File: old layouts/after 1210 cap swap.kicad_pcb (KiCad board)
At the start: 4 copper layers, 65 x 56 mm, 189 parts, among them J101 Conn_01x01, J102 Conn_01x01, J1101 USB_C_Receptacle, J401 +Vbat, J402 Gnd, J403 A, J404 B, J405 C, J406 Conn_01x03, K101 SERVO, P101 CANBUS, P102 CTRL_SIGNALS, P103 Serial1/tim4, P104 I2C, P106 HALL/Encoder, P801 SWD_DEBUG, P901 I2C, Q401 Q_PNP_BCE, Q501 TPH2R608NH,L1Q, Q502 TPH2R608NH,L1Q, Q503 TPH2R608NH,L1Q, Q504 TPH2R608NH,L1Q, Q601 TPH2R608NH,L1Q, Q602 TPH2R608NH,L1Q, Q603 TPH2R608NH,L1Q, Q604 TPH2R608NH,L1Q, Q701 TPH2R608NH,L1Q, Q702 TPH2R608NH,L1Q, Q703 TPH2R608NH,L1Q, Q704 TPH2R608NH,L1Q, SW801 SW_Push, U201 MAX3051, U301 TPS561201, U401 DRV8353RSRGZT, U801 STM32F40X_LQFP64, X801 8MHz 10ppm, X802 8MHz 10ppm

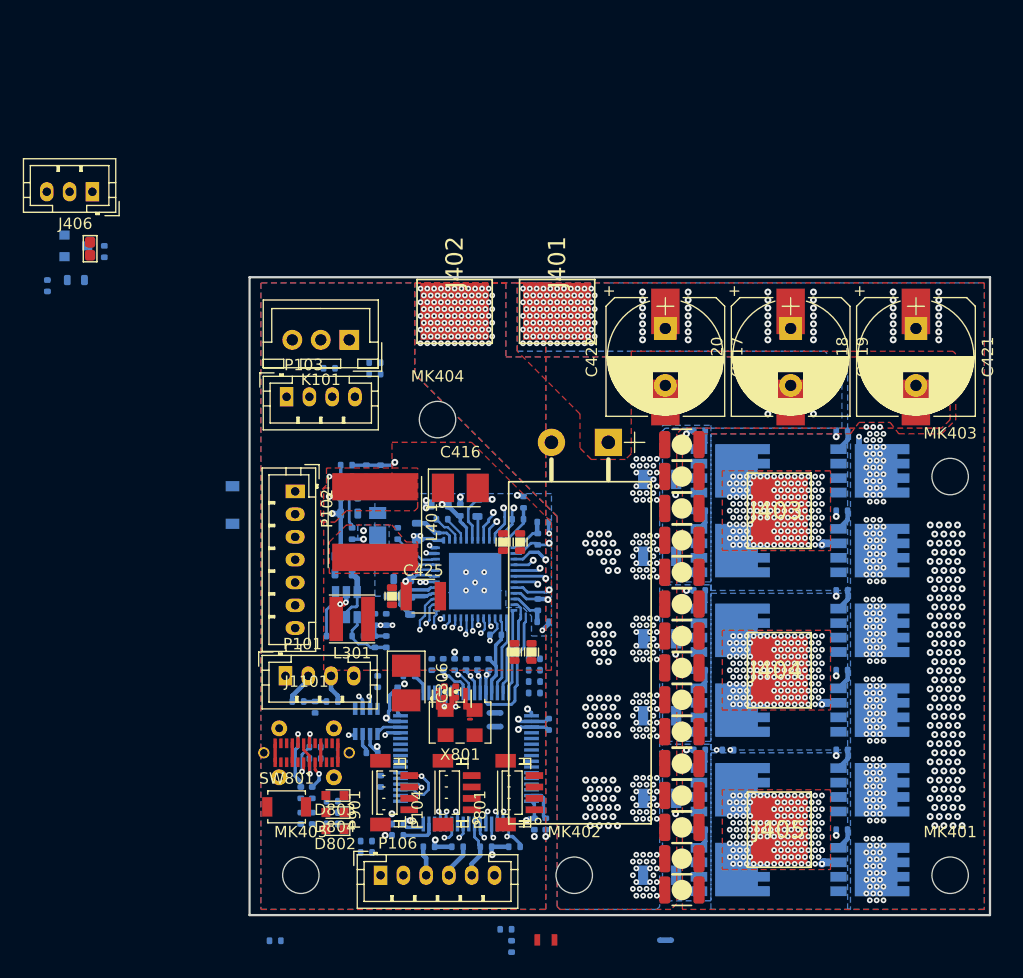
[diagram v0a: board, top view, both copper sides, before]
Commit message: connector layout basically finalised. drv gate layout finished mcu layout starting
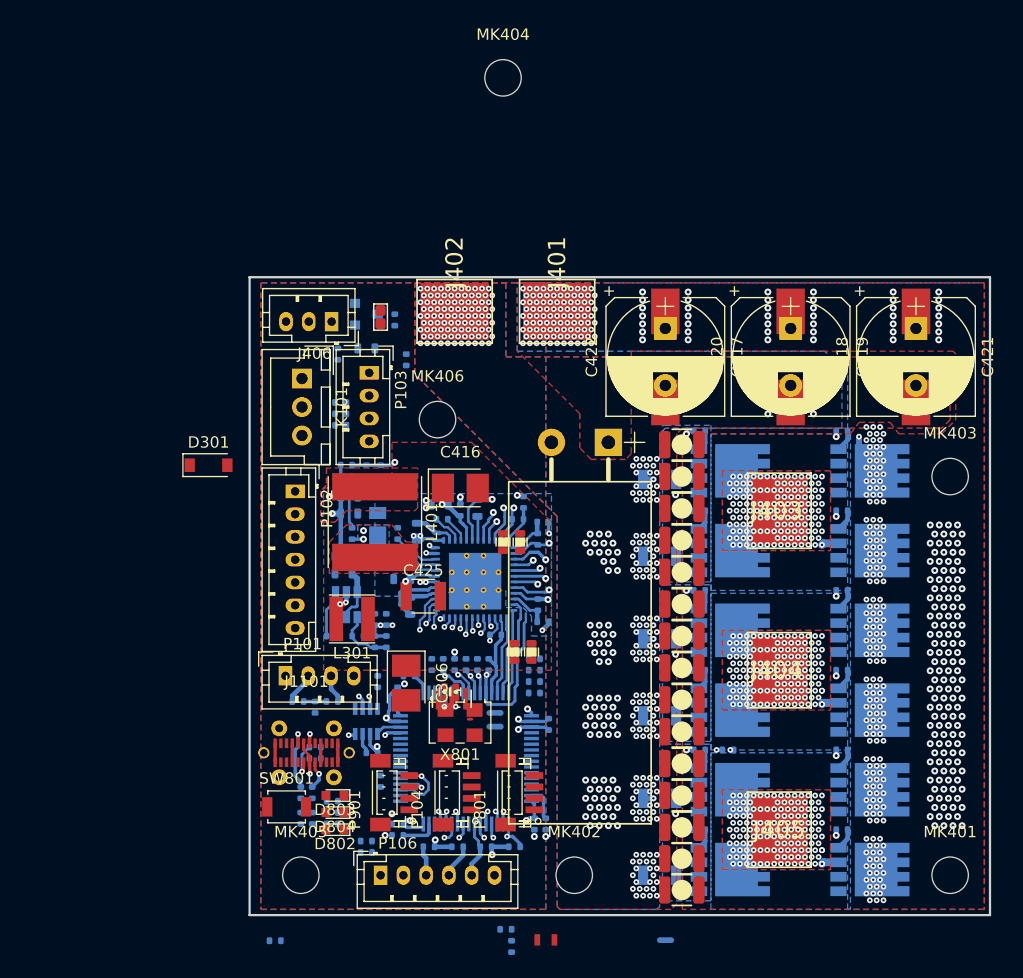
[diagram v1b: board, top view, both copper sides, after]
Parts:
- removed R421: 0Ω, pkl_dipol:R_0603
- added MK406: Mounting_Hole, Mounting_Holes:MountingHole_3.2mm_M3_DIN965, F.Cu at (121.0, 116.0)
- D301: moved to F.Cu
- R418: value 1M -> 10k
- moved MK404 30.5 mm to (126.8, 86.0)
- moved JP401 26.2 mm to (116.0, 107.0)
- moved Q401 26.2 mm to (114.8, 106.8)
- moved R418 26.2 mm to (117.2, 107.2)
- moved R419 26.2 mm to (114.8, 109.8)
- moved R420 26.2 mm to (112.2, 110.2)
- moved J406 23.9 mm to (111.7, 107.4)
- moved R403 20.8 mm to (118.2, 110.8), turned to 270 degrees
- moved P103 7.55 mm to (115.0, 111.9), turned to 270 degrees
- moved K101 5.36 mm to (109.1, 112.4), turned to 270 degrees
- moved R101 5.10 mm to (112.5, 116.5)
- moved C101 4.61 mm to (112.5, 115.5)
- moved R102 4.61 mm to (112.5, 114.5)
- moved D301 4.08 mm to (100.9, 120.0), turned to 0 degrees
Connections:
- net /ADC_BRAKE_R renamed Net-(P102-Pad4)
- net /ADC_THROTTLE_R renamed Net-(P102-Pad3)
- C404 pad 1: /drv_power_stage/BK_VIN -> +BATT
- C425 pad 1: /drv_power_stage/BK_VIN -> +BATT
- R403 pad 1: /drv_power_stage/BK_VIN -> /drv_power_stage/batt_pwr_ctl
- U401 pad 43: /drv_power_stage/BK_VIN -> +BATT
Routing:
- net /drv_power_stage/BK_VIN: track 3.12 -> 0.00 mm, vias 1 -> 0
- net +BATT: track 0.00 -> 3.12 mm, vias 463 -> 464
- net +15V: track 20.1 -> 20.8 mm, vias 4 -> 3
- net GNDD: vias 343 -> 338
- net /drv_power_stage/PHASE_C: vias 139 -> 145
- net /drv_power_stage/PHASE_B: vias 139 -> 145
- net /drv_power_stage/PHASE_A: vias 137 -> 143
